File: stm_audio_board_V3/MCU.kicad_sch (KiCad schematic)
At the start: 16 parts, among them J10 USB_A, SW1 SW_SPST, U1 IS42S16100H-7TL, U7 STM32H723ZGTx, Y2 X1E0000210132

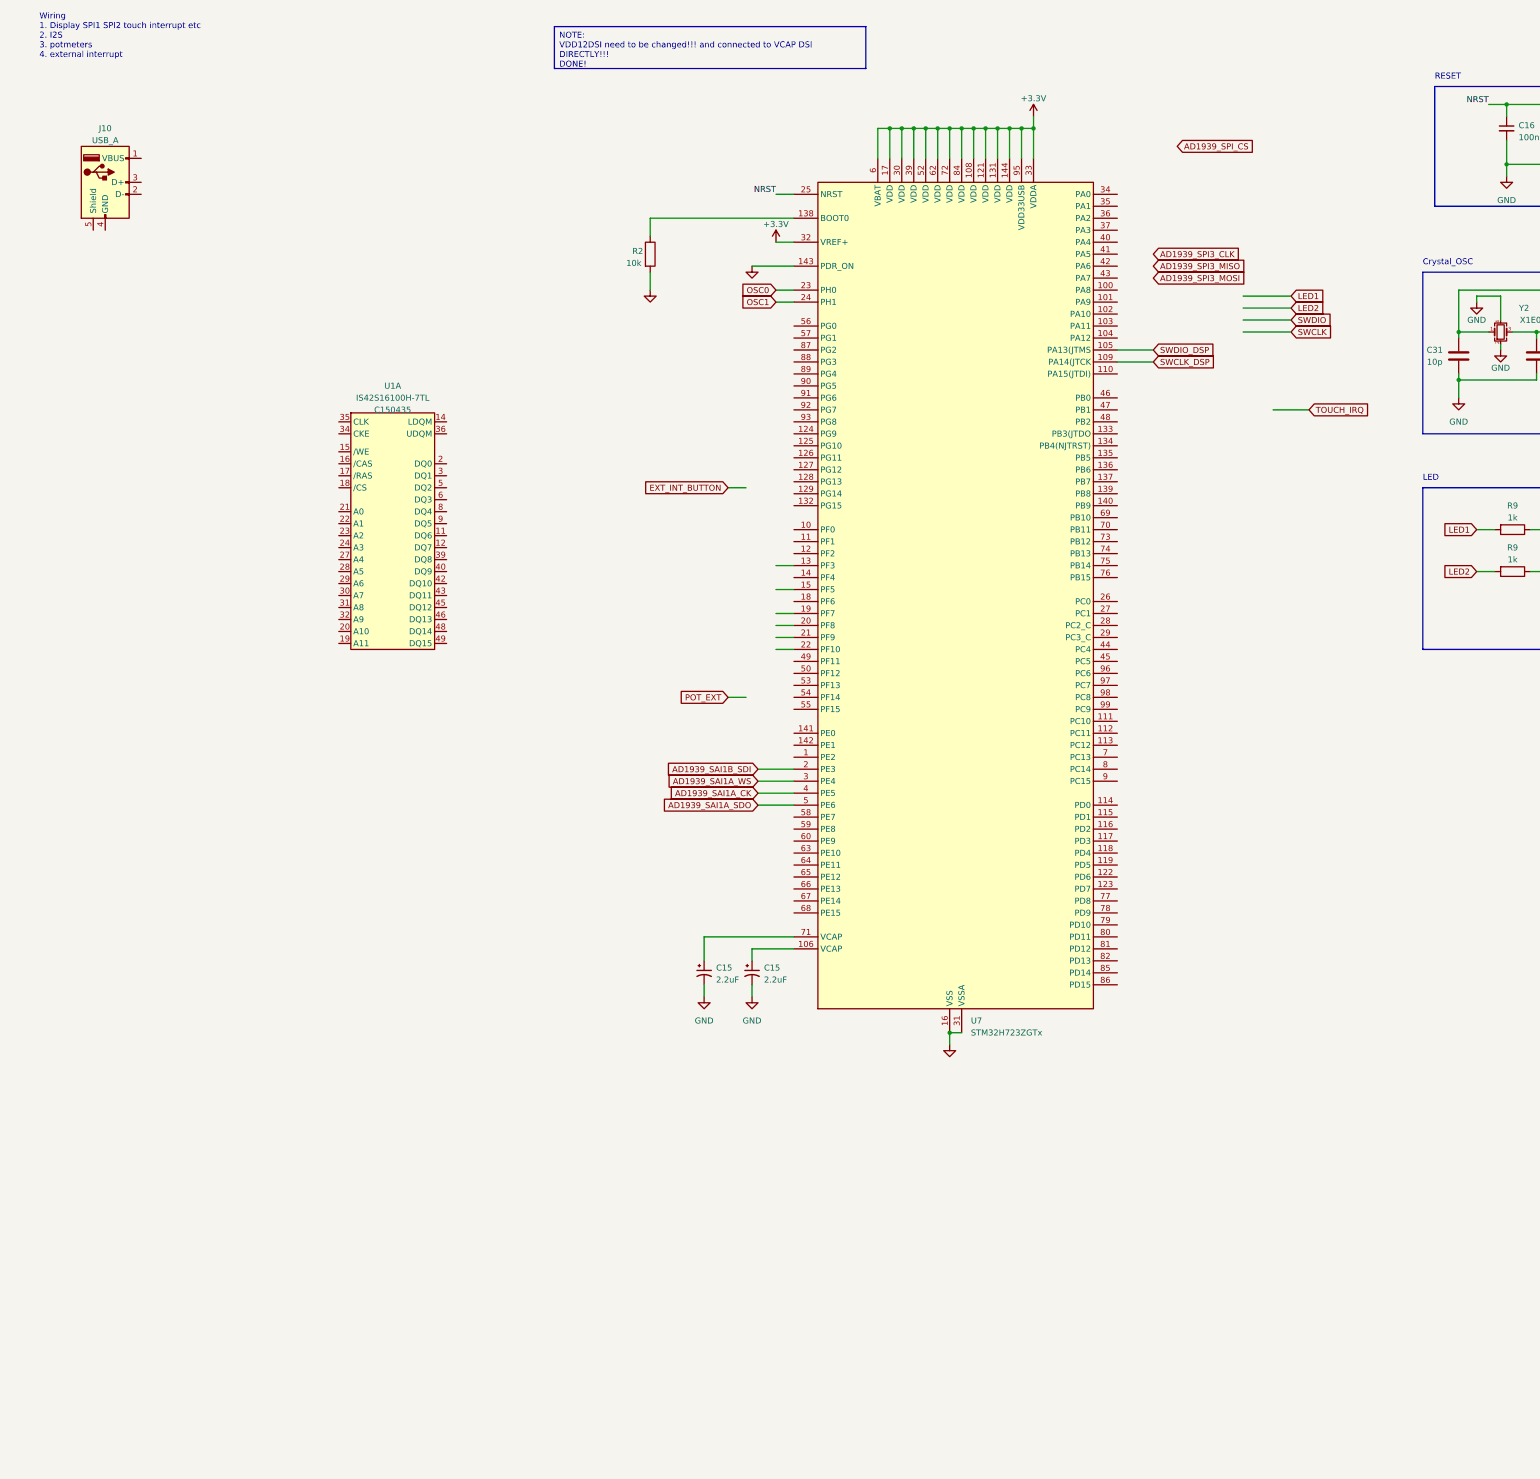
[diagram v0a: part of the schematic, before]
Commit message: Analog power and SDRAm routing reworked
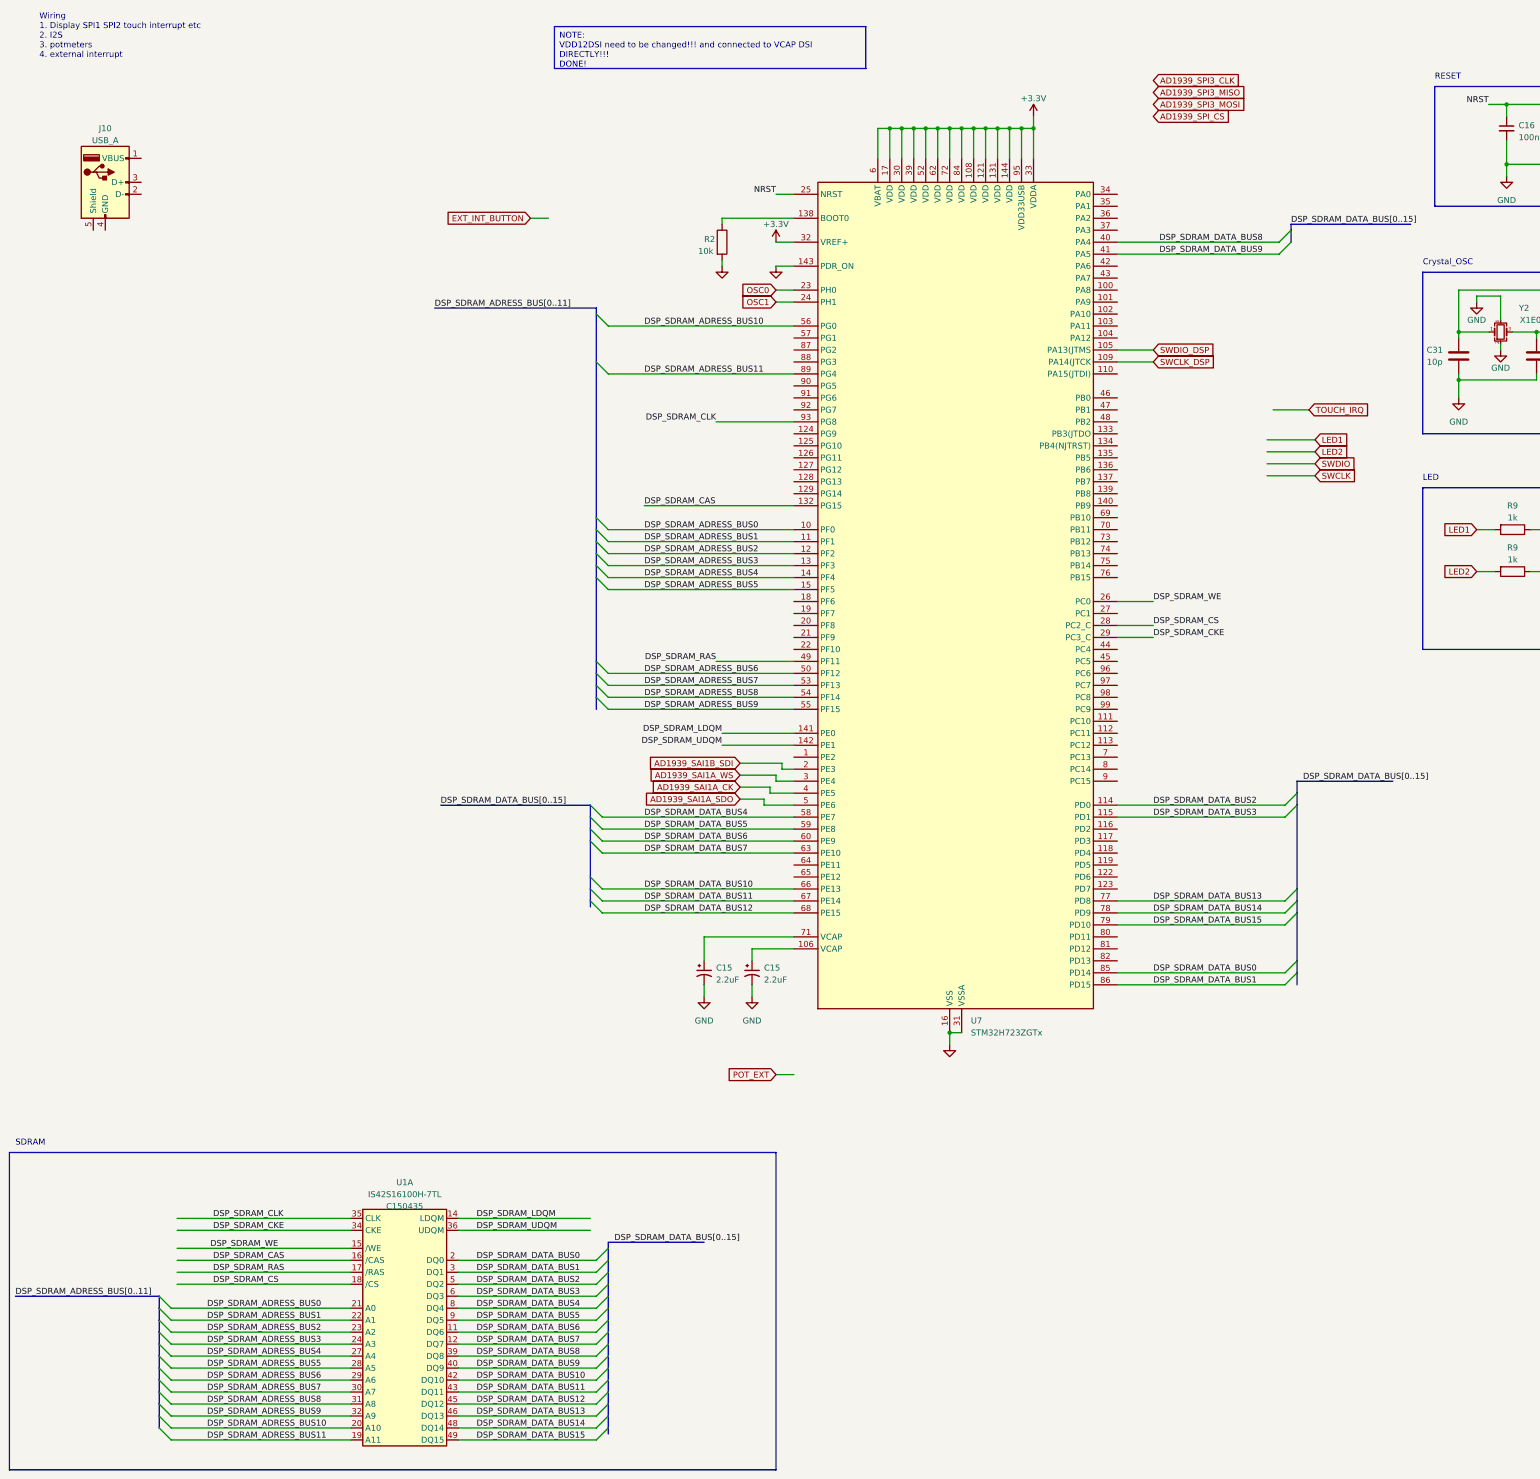
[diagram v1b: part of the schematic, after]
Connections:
- net DSP_SDRAM_DATA_BUS6: now reaches U1.11 (DQ6)
- net DSP_SDRAM_DATA_BUS6: now also U7.60 (PE9)
- net DSP_SDRAM_DATA_BUS7: now reaches U1.12 (DQ7)
- net DSP_SDRAM_DATA_BUS7: now also U7.63 (PE10)
- net DSP_SDRAM_LDQM: now reaches U1.14 (LDQM)
- net DSP_SDRAM_LDQM: now also U7.141 (PE0)
- net DSP_SDRAM_WE: now reaches U1.15 (/WE)
- net DSP_SDRAM_WE: now also U7.26 (PC0)
- net DSP_SDRAM_CAS: now reaches U1.16 (/CAS)
- net DSP_SDRAM_CAS: now also U7.132 (PG15)
- net DSP_SDRAM_RAS: now reaches U1.17 (/RAS)
- net DSP_SDRAM_RAS: now also U7.49 (PF11)
- net DSP_SDRAM_CS: now reaches U1.18 (/CS)
- net DSP_SDRAM_CS: now also U7.28 (PC2_C)
- net DSP_SDRAM_ADRESS_BUS11: now reaches U1.19 (A11)
- net DSP_SDRAM_ADRESS_BUS11: now also U7.89 (PG4)
- net DSP_SDRAM_DATA_BUS0: now reaches U1.2 (DQ0)
- net DSP_SDRAM_DATA_BUS0: now also U7.85 (PD14)
- net DSP_SDRAM_ADRESS_BUS10: now reaches U1.20 (A10)
- net DSP_SDRAM_ADRESS_BUS10: now also U7.56 (PG0)
- net DSP_SDRAM_ADRESS_BUS0: now reaches U1.21 (A0)
- net DSP_SDRAM_ADRESS_BUS0: now also U7.10 (PF0)
- net DSP_SDRAM_ADRESS_BUS1: now reaches U1.22 (A1)
- net DSP_SDRAM_ADRESS_BUS1: now also U7.11 (PF1)
- net DSP_SDRAM_ADRESS_BUS2: now reaches U1.23 (A2)
- net DSP_SDRAM_ADRESS_BUS2: now also U7.12 (PF2)
- net DSP_SDRAM_ADRESS_BUS3: now reaches U1.24 (A3)
- net DSP_SDRAM_ADRESS_BUS3: now also U7.13 (PF3)
- net DSP_SDRAM_ADRESS_BUS4: now reaches U1.27 (A4)
- net DSP_SDRAM_ADRESS_BUS4: now also U7.14 (PF4)
- net DSP_SDRAM_ADRESS_BUS5: now reaches U1.28 (A5)
- net DSP_SDRAM_ADRESS_BUS5: now also U7.15 (PF5)
- net DSP_SDRAM_ADRESS_BUS6: now reaches U1.29 (A6)
- net DSP_SDRAM_ADRESS_BUS6: now also U7.50 (PF12)
- net DSP_SDRAM_DATA_BUS1: now reaches U1.3 (DQ1)
- net DSP_SDRAM_DATA_BUS1: now also U7.86 (PD15)
- net DSP_SDRAM_ADRESS_BUS7: now reaches U1.30 (A7)
- net DSP_SDRAM_ADRESS_BUS7: now also U7.53 (PF13)
- net DSP_SDRAM_ADRESS_BUS8: now reaches U1.31 (A8)
- net DSP_SDRAM_ADRESS_BUS8: now also U7.54 (PF14)
- net DSP_SDRAM_ADRESS_BUS9: now reaches U1.32 (A9)
- net DSP_SDRAM_ADRESS_BUS9: now also U7.55 (PF15)
- net DSP_SDRAM_CKE: now reaches U1.34 (CKE)
- net DSP_SDRAM_CKE: now also U7.29 (PC3_C)
- net DSP_SDRAM_CLK: now reaches U1.35 (CLK)
- net DSP_SDRAM_CLK: now also U7.93 (PG8)
- net DSP_SDRAM_UDQM: now reaches U1.36 (UDQM)
- net DSP_SDRAM_UDQM: now also U7.142 (PE1)
- net DSP_SDRAM_DATA_BUS8: now reaches U1.39 (DQ8)
- net DSP_SDRAM_DATA_BUS8: now also U7.40 (PA4)
- net DSP_SDRAM_DATA_BUS9: now reaches U1.40 (DQ9)
- net DSP_SDRAM_DATA_BUS9: now also U7.41 (PA5)
- net DSP_SDRAM_DATA_BUS10: now reaches U1.42 (DQ10)
- net DSP_SDRAM_DATA_BUS10: now also U7.66 (PE13)
- net DSP_SDRAM_DATA_BUS11: now reaches U1.43 (DQ11)
- net DSP_SDRAM_DATA_BUS11: now also U7.67 (PE14)
- net DSP_SDRAM_DATA_BUS12: now reaches U1.45 (DQ12)
- net DSP_SDRAM_DATA_BUS12: now also U7.68 (PE15)
- net DSP_SDRAM_DATA_BUS13: now reaches U1.46 (DQ13)
- net DSP_SDRAM_DATA_BUS13: now also U7.77 (PD8)
- net DSP_SDRAM_DATA_BUS14: now reaches U1.48 (DQ14)
- net DSP_SDRAM_DATA_BUS14: now also U7.78 (PD9)
- net DSP_SDRAM_DATA_BUS15: now reaches U1.49 (DQ15)
- net DSP_SDRAM_DATA_BUS15: now also U7.79 (PD10)
- net DSP_SDRAM_DATA_BUS2: now reaches U1.5 (DQ2)
- net DSP_SDRAM_DATA_BUS2: now also U7.114 (PD0)
- net DSP_SDRAM_DATA_BUS3: now reaches U1.6 (DQ3)
- net DSP_SDRAM_DATA_BUS3: now also U7.115 (PD1)
- net DSP_SDRAM_DATA_BUS4: now reaches U1.8 (DQ4)
- net DSP_SDRAM_DATA_BUS4: now also U7.58 (PE7)
- net DSP_SDRAM_DATA_BUS5: now reaches U1.9 (DQ5)
- net DSP_SDRAM_DATA_BUS5: now also U7.59 (PE8)
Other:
- note added: "SDRAM"
- moved on the sheet: R2, U1A
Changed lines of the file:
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@@
 (kicad_sch (version 20230121) (generator eeschema)
-  (paper "A3")
+  (paper "A2")

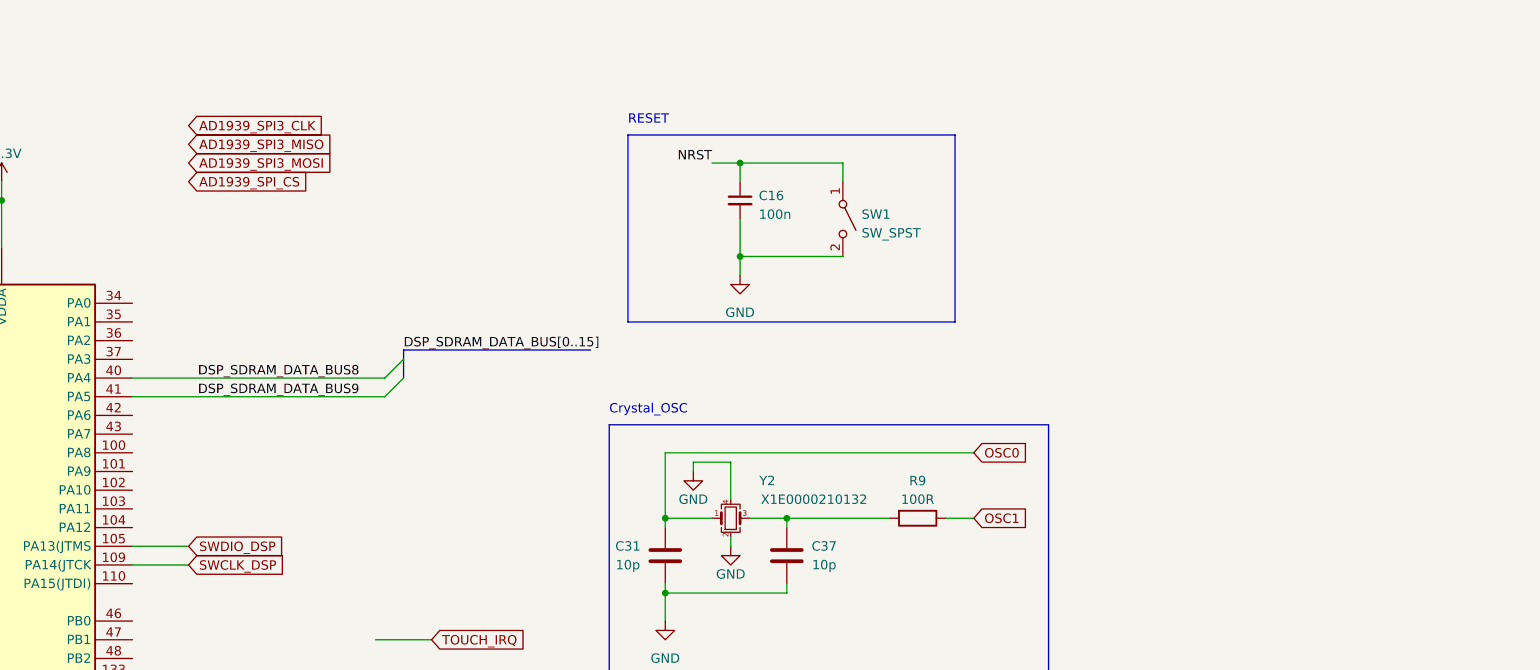
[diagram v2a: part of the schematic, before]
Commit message: USB added
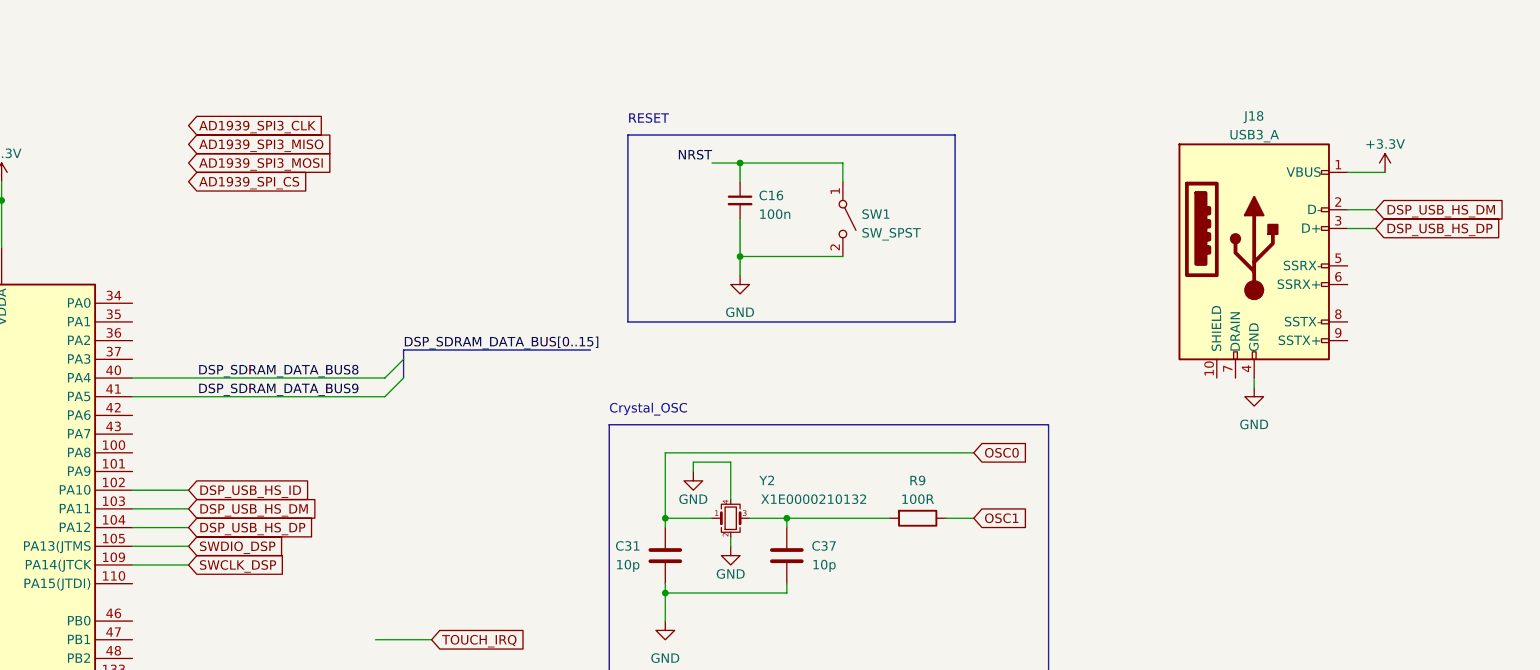
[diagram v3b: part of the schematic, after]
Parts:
- added J18: USB3_A, Connector_USB:USB3_A_Receptacle_Wuerth_692122030100, symbol Connector:USB3_A
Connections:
- net +3.3V: now also J18.1 (VBUS)
- net GND: now also J18.4 (GND)
- net DSP_USB_HS_ID: now reaches U7.102 (PA10)
- net DSP_USB_HS_DM: now reaches U7.103 (PA11)
- net DSP_USB_HS_DM: now also J18.2 (D-)
- net DSP_USB_HS_DP: now reaches U7.104 (PA12)
- net DSP_USB_HS_DP: now also J18.3 (D+)

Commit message: New orientation, Overvoltage protection added
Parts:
- removed J18: USB3_A, Connector_USB:USB3_A_Receptacle_Wuerth_692122030100, symbol Connector:USB3_A
- added C16: 100n, Capacitor_SMD:C_0603_1608Metric, symbol Device:C_Small
- added U16: USBLC6-2P6, Package_TO_SOT_SMD:SOT-666, symbol Power_Protection:USBLC6-2P6
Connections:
- net +3.3V: now also J10.1 (VBUS), C16.1, U16.5 (VBUS)
- net DSP_USB_HS_DM: now also U16.6 (I/O1)
- net DSP_USB_HS_DP: now also U16.4 (I/O2)
- net GND: now also J10.4 (GND), C16.2, U16.2 (GND)
- net USB_Conn_D-: now reaches J10.2 (D-)
- net USB_Conn_D-: now also U16.1 (I/O1)
- net USB_Conn_D+: now reaches J10.3 (D+)
- net USB_Conn_D+: now also U16.3 (I/O2)

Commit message: Testpoints and parts for usb hub added
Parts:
- added C12 (x20): 100n, Capacitor_SMD:C_0603_1608Metric, symbol Device:C_Small
- added C16 (x2): 20P, Capacitor_SMD:C_0402_1005Metric, symbol Device:C_Small
- added U17: W25Q128JVS, Package_SO:SOIC-8_5.23x5.23mm_P1.27mm, symbol Memory_Flash:W25Q128JVS
- added U19: FE1.1s, Package_SO:SSOP-28_3.9x9.9mm_P0.635mm, symbol Interface_USB:FE1.1s
- added Y3: Crystal_GND24, Crystal:Crystal_SMD_3225-4Pin_3.2x2.5mm, symbol Device:Crystal_GND24
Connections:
- net +3.3V: now also C12.1, C12.1, C12.1, C12.1, C12.1, C12.1, C12.1, C12.1, C12.1, C12.1, C12.1, C12.1, C12.1, C12.1, C12.1, C12.1, C12.1, C12.1, C12.1, C12.1, U17.8 (VCC), U19.13 (VD33), U19.18 (VBUSM)
- net GND: now also C12.2, C12.2, C12.2, C12.2, C12.2, C12.2, C12.2, C12.2, C12.2, C12.2, C12.2, C12.2, C12.2, C12.2, C12.2, C12.2, C12.2, C12.2, C12.2, C12.2, C16.1, C16.2, U17.4 (GND), U19.1 (VSS), Y3.2, Y3.4
- net DSP_FLASH_D2: now reaches U7.1 (PE2)
- net DSP_FLASH_D2: now also U17.3 (IO2)
- net DSP_FLASH_D3: now reaches U7.18 (PF6)
- net DSP_FLASH_D3: now also U17.7 (IO3)
- net DSP_FLASH_D0: now reaches U7.20 (PF8)
- net DSP_FLASH_D0: now also U17.5 (DI(IO0))
- net DSP_FLASH_D1: now reaches U7.21 (PF9)
- net DSP_FLASH_D1: now also U17.2 (DO(IO1))
- net DSP_FLASH_CLK: now reaches U7.22 (PF10)
- net DSP_FLASH_CLK: now also U17.6 (CLK)
- net DSP_FLASH_CS: now reaches U7.64 (PE11)
- net DSP_FLASH_CS: now also U17.1 (~{CS})
- net DSP_USB_HS_DM: no longer names the net of U16.6 (I/O1)
- net DSP_USB_HS_DM: now also U19.16 (DPU); no longer U7.103 (PA11)
- net DSP_USB_HS_DP: no longer names the net of U16.4 (I/O2)
- net DSP_USB_HS_DP: now also U19.15 (DMU); no longer U7.104 (PA12)
- net DSP_USB_HS_ID: no longer names the net of U7.102 (PA10)
- new net: C16.1, U19.3 (XIN), Y3.1
- new net: C16.2, U19.2 (XOUT), Y3.3
- new net DISPLAY_USB_HS_D+: U19.9 (DP2)
- new net DISPLAY_USB_HS_D-: U19.8 (DM2)
- new net DSP_USB_HS_D+: U19.11 (DP1), U7.104 (PA12)
- new net DSP_USB_HS_D-: U19.10 (DM1), U7.103 (PA11)
- no-connect marks 0 -> 4
